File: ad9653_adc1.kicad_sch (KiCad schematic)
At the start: 24 parts, among them J701 SMA, J702 SMA, J703 SMA, J704 SMA, U701 AD9653BCPZ-125

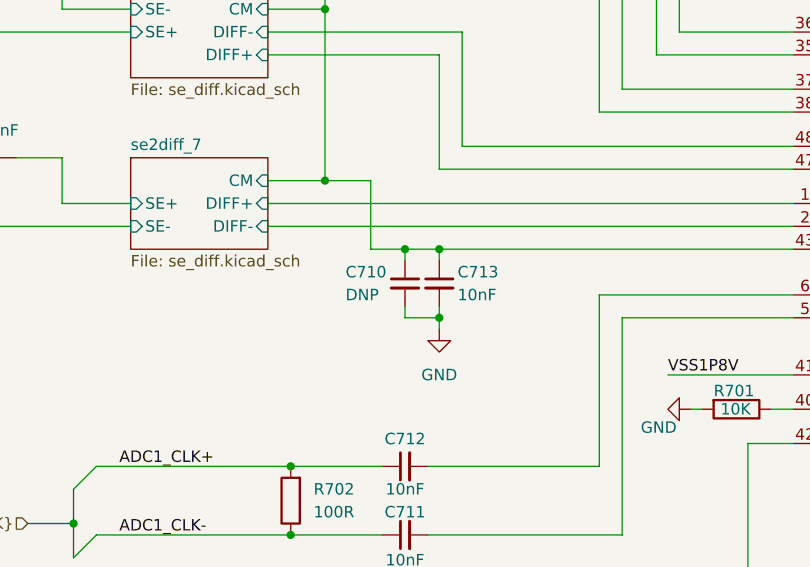
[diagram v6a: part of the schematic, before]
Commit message: Properly attributed DNP parts; Added Fabrication Notes
-Properly attributed various DNP in the project;
This includes: C210.C710,C1601,C2502,C2602,L2501,R1507,L2601,R1601,R805
- I changed the accelerometer and microphone (+it's filter)to DNP parts
  Note: both of these are obsolete parts. As part of this change I Changed R1602 (part of mic buffer) from 220k to 0R. The removal of these parts should in no way negatively effect the rest of the circuit.
-I fixed the 'value' attribute of XMER2501&XMER2601 from 'TC4-6+' -> 'TC4-6T+'
- I added some fabrication notes to the F.Fab Layer
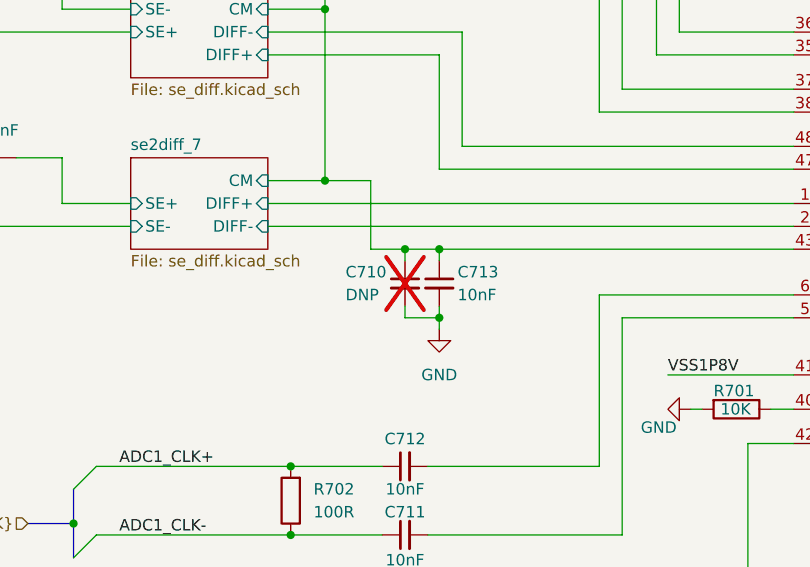
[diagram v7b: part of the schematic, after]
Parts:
- C710: now not fitted
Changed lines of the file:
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@@
 		(in_bom yes)
 		(on_board yes)
-		(dnp no)
+		(dnp yes)
 		(property "Reference" "C710"
 			(at 153.416 165.1 0)

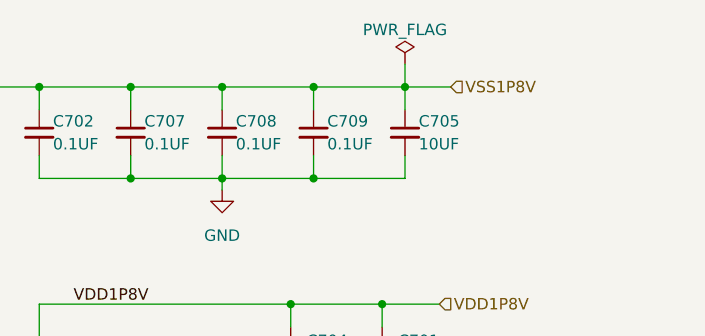
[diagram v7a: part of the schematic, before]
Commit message: resolve duplicate power flag
kicad 8 complains about two power flags on VSS1P8V net,
one each on ADC0 and ADC1 pages.  Consolidate to one
flag on the U35_LT6233 page.
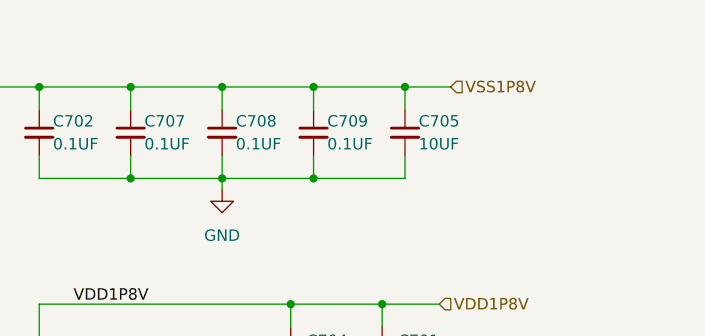
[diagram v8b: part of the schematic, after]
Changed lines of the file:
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@@
-	(wire
-		(pts
-			(xy 271.78 73.66) (xy 271.78 76.2)
-		)
-		(stroke
-			(width 0)
-			(type default)
-		)
-	)
 	(wire
 		(pts
@@
 					(unit 1)
 				)
-			)
-		)
-	)
-	(symbol
-		(lib_id "power:PWR_FLAG")
-		(at 271.78 73.66 0)
-		(mirror y)
-		(unit 1)
-		(exclude_from_sim no)
-		(in_bom yes)
-		(on_board yes)
-		(dnp no)
-		(property "Reference" "#FLG05"
-			(at 271.78 71.755 0)
-			(effects
-				(font
-					(size 1.27 1.27)
-				)
-				(hide yes)
-			)
-		)
-		(property "Value" "PWR_FLAG"
-			(at 271.78 69.85 0)
-			(effects
-				(font
-					(size 1.27 1.27)
-				)
-			)
-		)
-		(property "Footprint" ""
-			(at 271.78 73.66 0)
-			(effects
-				(font
-					(size 1.27 1.27)
-				)
-				(hide yes)
-			)
-		)
-		(property "Datasheet" "~"
-			(at 271.78 73.66 0)
-			(effects
-				(font
-					(size 1.27 1.27)
-				)
-				(hide yes)
-			)
-		)
-		(property "Description" "Special symbol for telling ERC where power comes from"
-			(at 271.78 73.66 0)
-			(effects
-				(font
-					(size 1.27 1.27)
-				)
-				(hide yes)
-			)
-		)
-		(pin "1"
-		)
-		(instances
-			(project "zest"
-				(path "/00000000-0000-0000-0000-000000000003/00000000-0000-0000-0000-000000000001"
-					(reference "#FLG05")
-					(unit 1)
-				)
